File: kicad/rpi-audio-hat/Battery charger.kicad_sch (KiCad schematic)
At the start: 16 parts, among them J6 USB_C_Receptacle_USB2.0, U10 FUSB303BTMX, U3 SLM6800

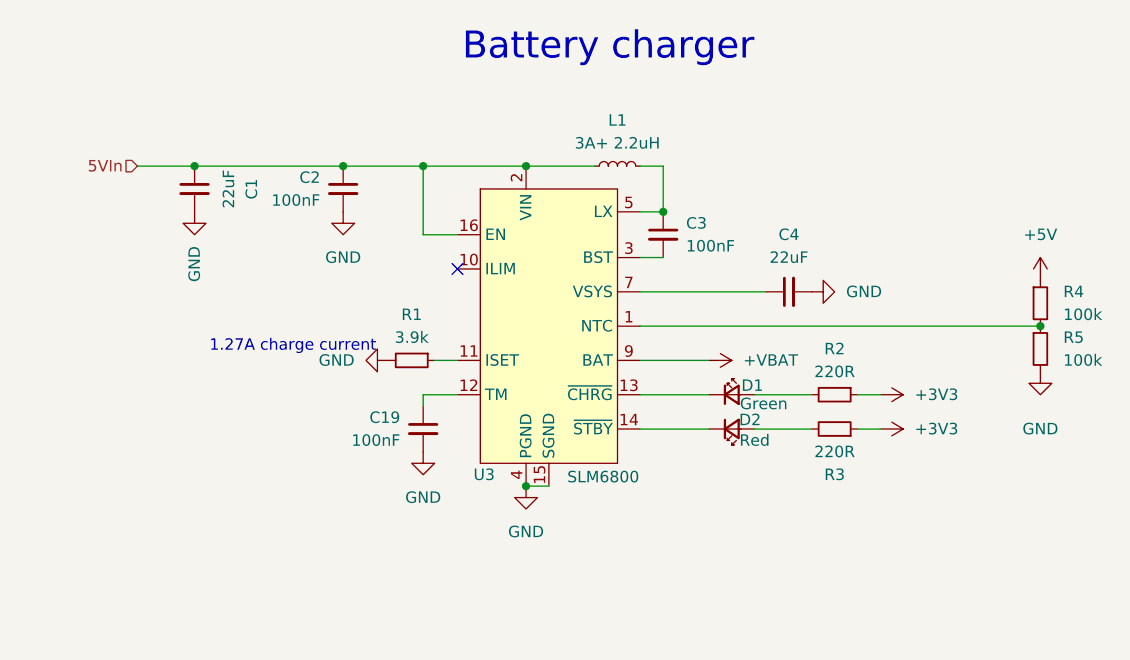
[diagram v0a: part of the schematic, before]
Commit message: Fix power switch & symbol update
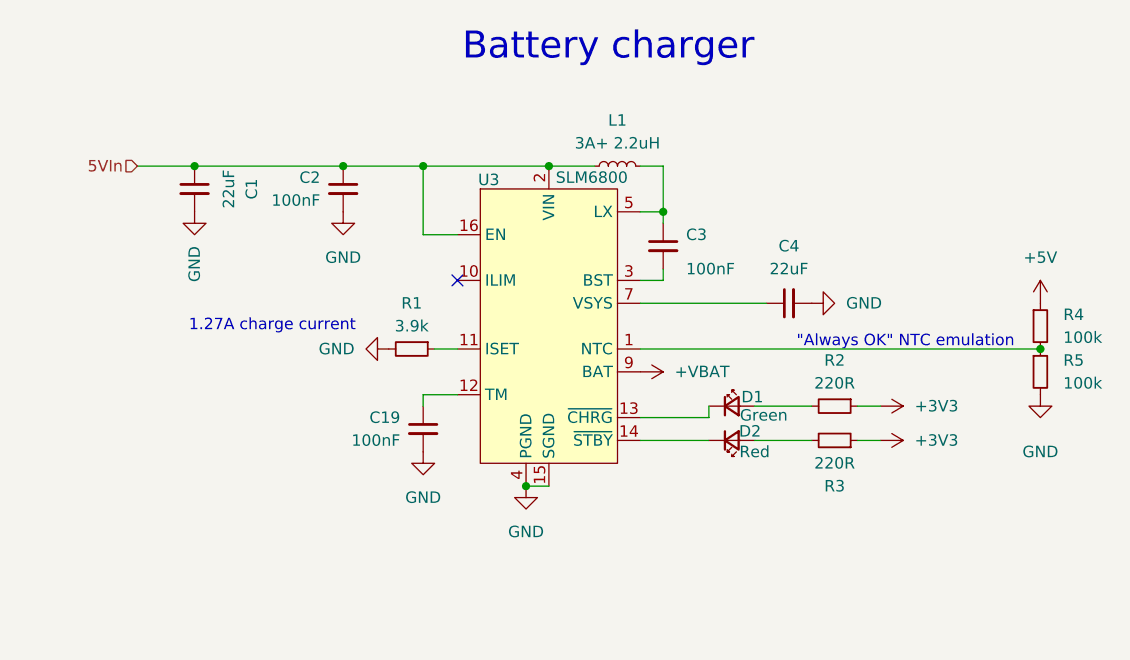
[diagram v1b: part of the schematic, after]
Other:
- note added: ""Always OK" NTC emulation"
- moved on the sheet: C3, C4, D1, D2, R1, R2, R3, R4, R5
